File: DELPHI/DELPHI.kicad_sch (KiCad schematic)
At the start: 86 parts, among them SW1 SW_Push_45deg, SW10 SW_Push_45deg, SW11 SW_Push_45deg, SW12 SW_Push_45deg, SW13 SW_Push_45deg, SW14 SW_Push_45deg, SW15 SW_Push_45deg, SW16 SW_Push_45deg, SW17 SW_Push_45deg, SW18 SW_Push_45deg, SW19 SW_Push_45deg, SW2 SW_Push_45deg, SW20 SW_Push_45deg, SW21 SW_Push_45deg, SW22 SW_Push_45deg, SW23 SW_Push_45deg, SW24 SW_Push_45deg, SW25 SW_Push_45deg, SW26 SW_Push_45deg, SW27 SW_Push_45deg, SW28 SW_Push_45deg, SW29 SW_Push_45deg, SW3 SW_Push_45deg, SW30 SW_Push_45deg, SW31 SW_Push_45deg, SW32 SW_Push_45deg, SW33 SW_Push_45deg, SW34 SW_Push_45deg, SW35 SW_Push_45deg, SW36 SW_Push_45deg, SW37 SW_Push_45deg, SW38 SW_Push_45deg, SW39 SW_Push_45deg, SW4 SW_Push_45deg, SW40 SW_Push_45deg, SW41 SW_Push_45deg, SW42 SW_Push_45deg, SW5 SW_Push_45deg, SW6 SW_Push_45deg, SW7 SW_Push_45deg, SW8 SW_Push_45deg, SW9 SW_Push_45deg, U1 QTPy, U2 QTPy

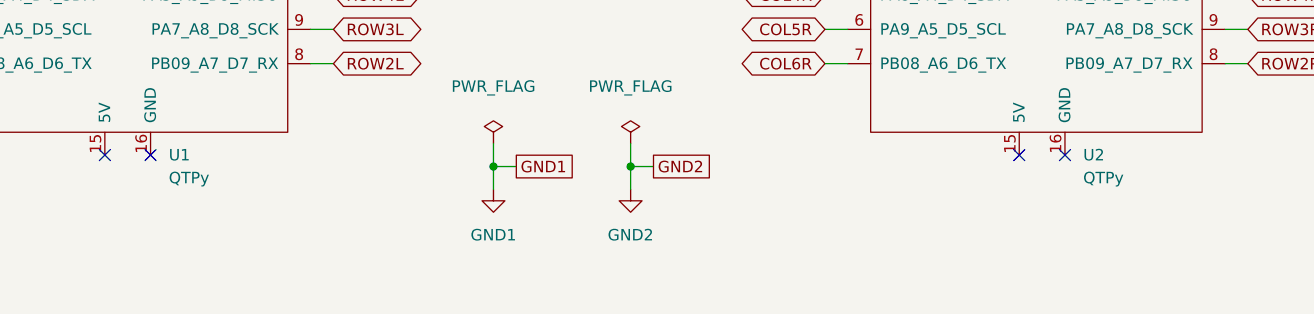
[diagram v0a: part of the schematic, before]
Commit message: Update DELPHI.kicad_sch
Update title block
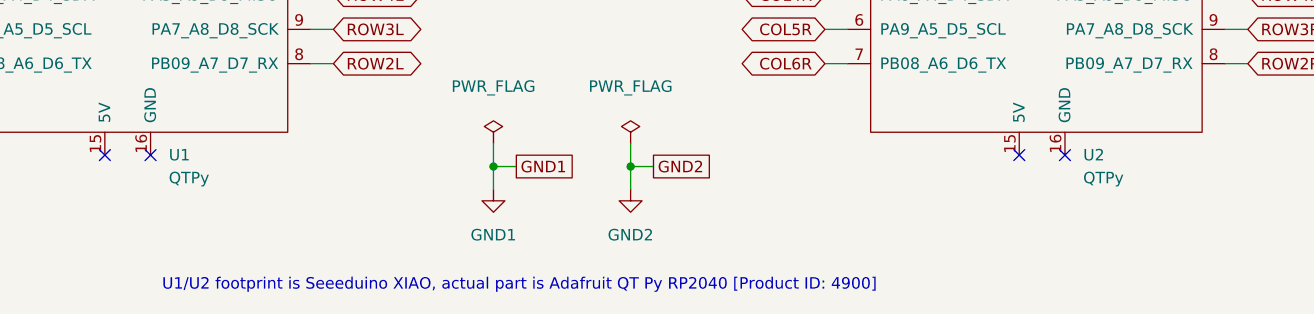
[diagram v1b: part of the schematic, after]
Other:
- note added: "U1/U2 footprint is Seeeduino XIAO, actual part is Adafruit QT Py RP2040 [Product ID: 4900]"
- company: (none) -> John A. Riggles
- title: (none) -> D.E.L.P.H.I [Dual Ergolinear Low-Profile Human Interface]
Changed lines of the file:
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@@
 (kicad_sch (version 20211123) (generator eeschema)
   (paper "USLedger")
+  (title_block
+    (title "D.E.L.P.H.I [Dual Ergolinear Low-Profile Human Interface]")
+    (date "2022-12-01")
+    (rev "1.0")
+    (company "John A. Riggles")
+  )
   (junction (at 152.4 76.2) (diameter 0) (color 0 0 0 0)
   )
@@
     (stroke (width 0) (type default) (color 0 0 0 0))
   )
+  (text "U1/U2 footprint is Seeeduino XIAO, actual part is Adafruit QT Py RP2040 [Product ID: 4900]"
+    (at 73.66 184.15 0)
+    (effects (font (size 1.27 1.27)) (justify left bottom))
+  )
   (global_label "COL1R" (shape bidirectional) (at 127 34.29 90) (fields_autoplaced)
